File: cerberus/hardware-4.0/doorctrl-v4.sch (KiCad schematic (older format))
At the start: 6 parts, among them CON1 AVR-ISP-6, CON2 AVR-JTAG-10, IC1 ATMEGA324P-A, X1 12 MHz

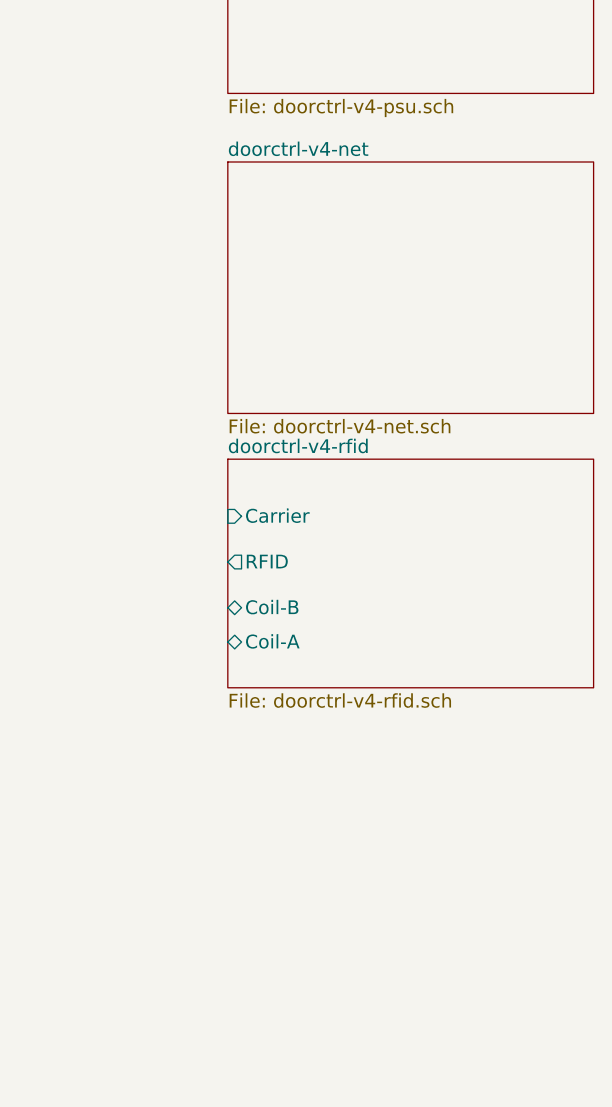
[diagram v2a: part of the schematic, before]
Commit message: Added RS-485 transciever and connectors
git-svn-id: file:///home/ff/projects/osaa/svn@216 a092026d-3e22-4cff-94a7-eaa6fdd35d37
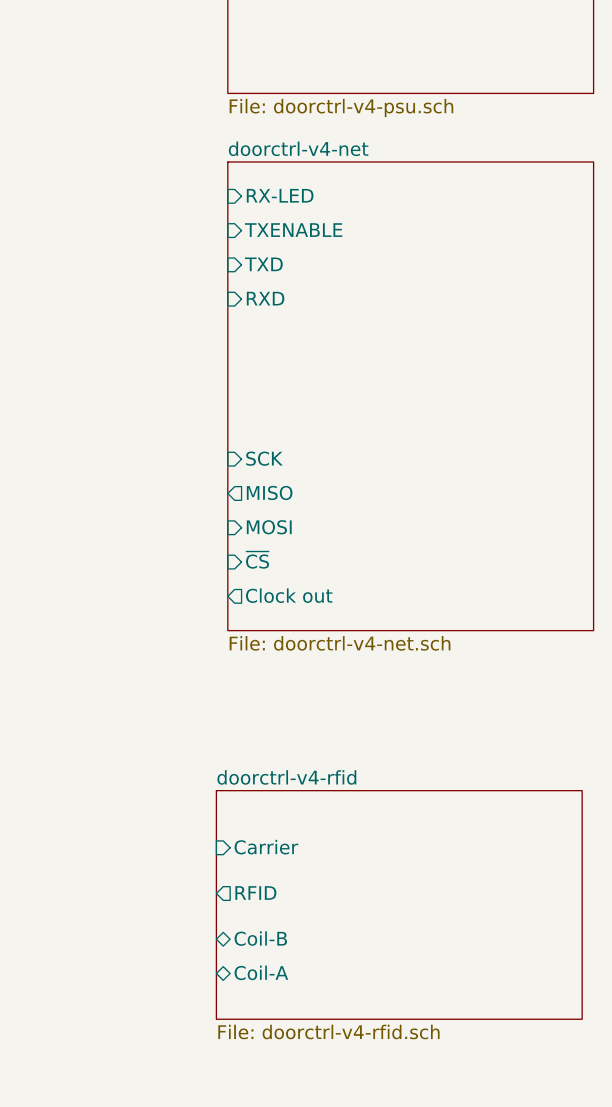
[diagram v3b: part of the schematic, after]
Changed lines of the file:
@@
-EESchema Schematic File Version 2  date 2010-12-15T21:23:41 CET
+EESchema Schematic File Version 2  date 2010-12-16T22:33:40 CET
 LIBS:enc28j60
 LIBS:power
@@
 LIBS:g5sb
 LIBS:pulse-pe-68517-ethernet-trafo
+LIBS:sn65hvd1x
 LIBS:doorctrl-v4-cache
 EELAYER 24  0
@@
 Sheet 1 5
 Title ""
-Date "15 dec 2010"
+Date "16 dec 2010"
 Rev ""
 Comp ""
@@
 $EndSheet
 $Sheet
-S 9300 3400 1600 1000
+S 9250 4850 1600 1000
 U 4CFD3072
 F0 "doorctrl-v4-rfid" 60
 F1 "doorctrl-v4-rfid.sch" 60
-F2 "RFID" O L 9300 3850 60
-F3 "Coil-B" B L 9300 4050 60
-F4 "Coil-A" B L 9300 4200 60
-F5 "Carrier" I L 9300 3650 60
+F2 "RFID" O L 9250 5300 60
+F3 "Coil-B" B L 9250 5500 60
+F4 "Coil-A" B L 9250 5650 60
+F5 "Carrier" I L 9250 5100 60
 $EndSheet
 $Sheet
@@
 $EndSheet
 $Sheet
-S 9300 2100 1600 1100
+S 9300 2100 1600 2050
 U 4CFD2FB8
 F0 "doorctrl-v4-net" 60
 F1 "doorctrl-v4-net.sch" 60
+F2 "RX-LED" I L 9300 2250 60
+F3 "TXENABLE" I L 9300 2400 60
+F4 "TXD" I L 9300 2550 60
+F5 "RXD" I L 9300 2700 60
+F6 "SCK" I L 9300 3400 60
+F7 "MISO" O L 9300 3550 60
+F8 "MOSI" I L 9300 3700 60
+F9 "~CS" I L 9300 3850 60
+F10 "Clock out" O L 9300 4000 60
 $EndSheet
 NoConn ~ 3300 5900
@@
 PB5
 $Comp
-L +3.3V #PWR01
+L +3.3V #PWR4
 U 1 1 4CFAB301
 P 2150 2275
-F 0 "#PWR01" H 2150 2235 30  0001 C CNN
+F 0 "#PWR4" H 2150 2235 30  0001 C CNN
 F 1 "+3.3V" H 2150 2385 30  0000 C CNN
 	1    2150 2275
@@
 $EndComp
 $Comp
-L GND #PWR02
+L GND #PWR3
 U 1 1 4CFAB0A0
 P 1850 2475
-F 0 "#PWR02" H 1850 2475 30  0001 C CNN
+F 0 "#PWR3" H 1850 2475 30  0001 C CNN
 F 1 "GND" H 1850 2405 30  0001 C CNN
 	1    1850 2475
@@
 $EndComp
 $Comp
-L GND #PWR03
+L GND #PWR1
 U 1 1 4CFAB098
 P 1050 2475
-F 0 "#PWR03" H 1050 2475 30  0001 C CNN
+F 0 "#PWR1" H 1050 2475 30  0001 C CNN
 F 1 "GND" H 1050 2405 30  0001 C CNN
 	1    1050 2475
@@
 PC2
 $Comp
-L +3.3V #PWR04
+L +3.3V #PWR7
 U 1 1 4CFA7FD7
 P 3675 5700
-F 0 "#PWR04" H 3675 5660 30  0001 C CNN
+F 0 "#PWR7" H 3675 5660 30  0001 C CNN
 F 1 "+3.3V" H 3675 5810 30  0000 C CNN
 	1    3675 5700
@@
 $EndComp
 $Comp
-L +3.3V #PWR05
+L +3.3V #PWR2
 U 1 1 4CFA5CC7
 P 1800 5600
-F 0 "#PWR05" H 1800 5560 30  0001 C CNN
+F 0 "#PWR2" H 1800 5560 30  0001 C CNN
 F 1 "+3.3V" H 1800 5710 30  0000 C CNN
 	1    1800 5600
@@
 RESET
 $Comp
-L GND #PWR06
+L GND #PWR5
 U 1 1 4CF6BFD7
 P 3050 5075
-F 0 "#PWR06" H 3050 5075 30  0001 C CNN
+F 0 "#PWR5" H 3050 5075 30  0001 C CNN
 F 1 "GND" H 3050 5005 30  0001 C CNN
 	1    3050 5075
@@
 $EndComp
 $Comp
-L +3.3V #PWR07
+L +3.3V #PWR6
 U 1 1 4CF6BFC6
 P 3125 675
-F 0 "#PWR07" H 3125 635 30  0001 C CNN
+F 0 "#PWR6" H 3125 635 30  0001 C CNN
 F 1 "+3.3V" H 3125 785 30  0000 C CNN
 	1    3125 675

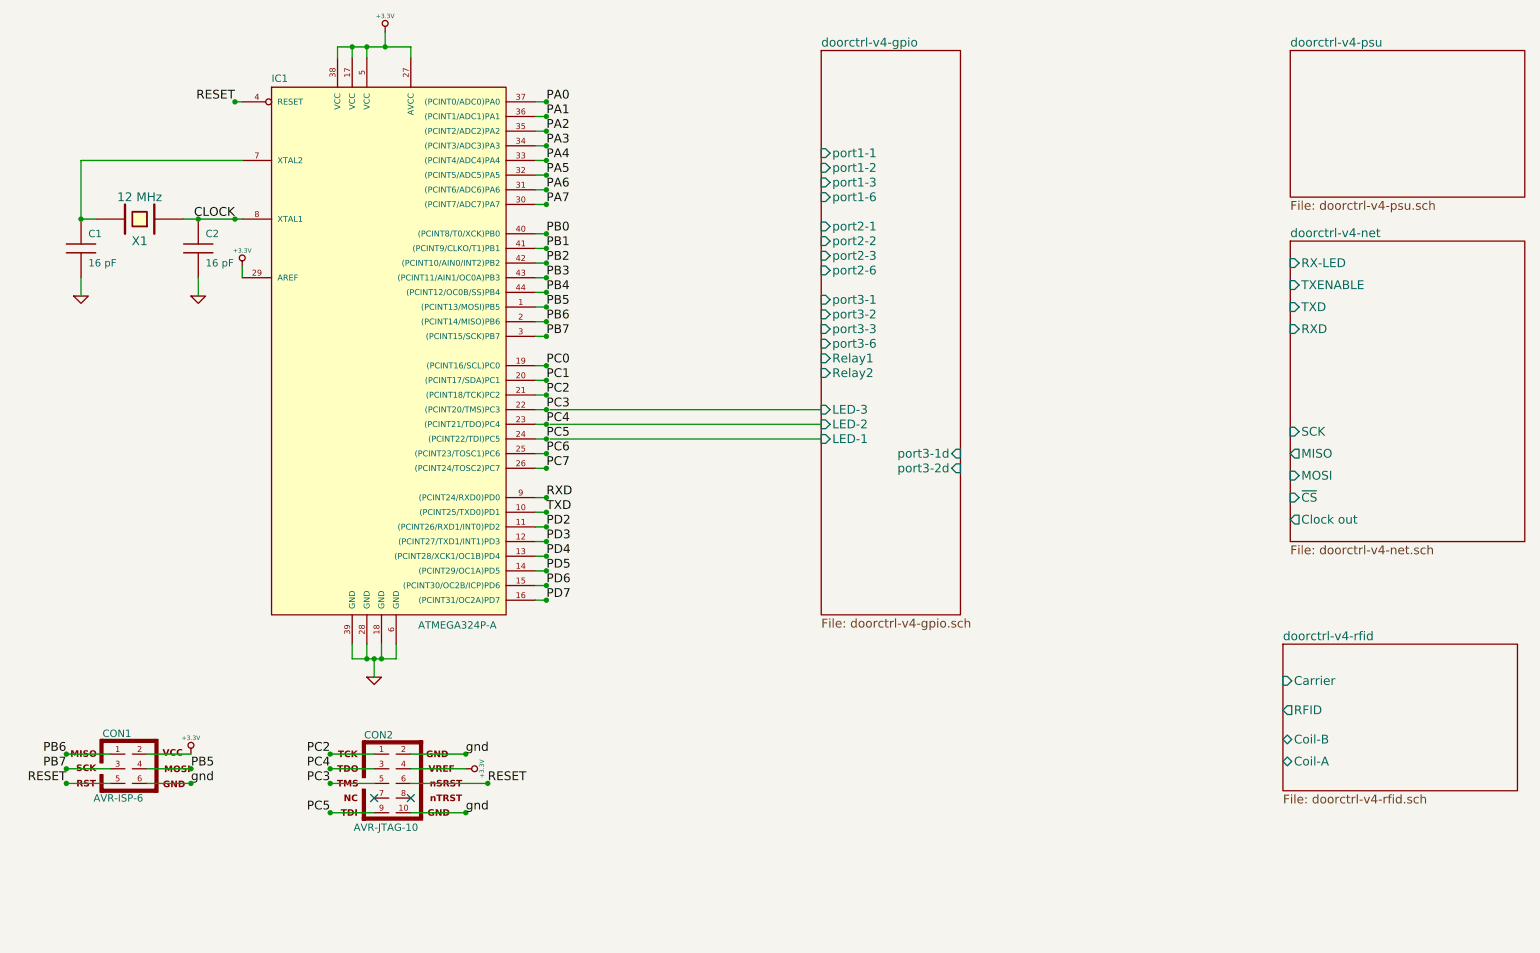
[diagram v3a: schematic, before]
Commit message: Added a 5V regulator for most stuff, except ENC28J60 which lives on its own 3.3v supply
git-svn-id: file:///home/ff/projects/osaa/svn@217 a092026d-3e22-4cff-94a7-eaa6fdd35d37
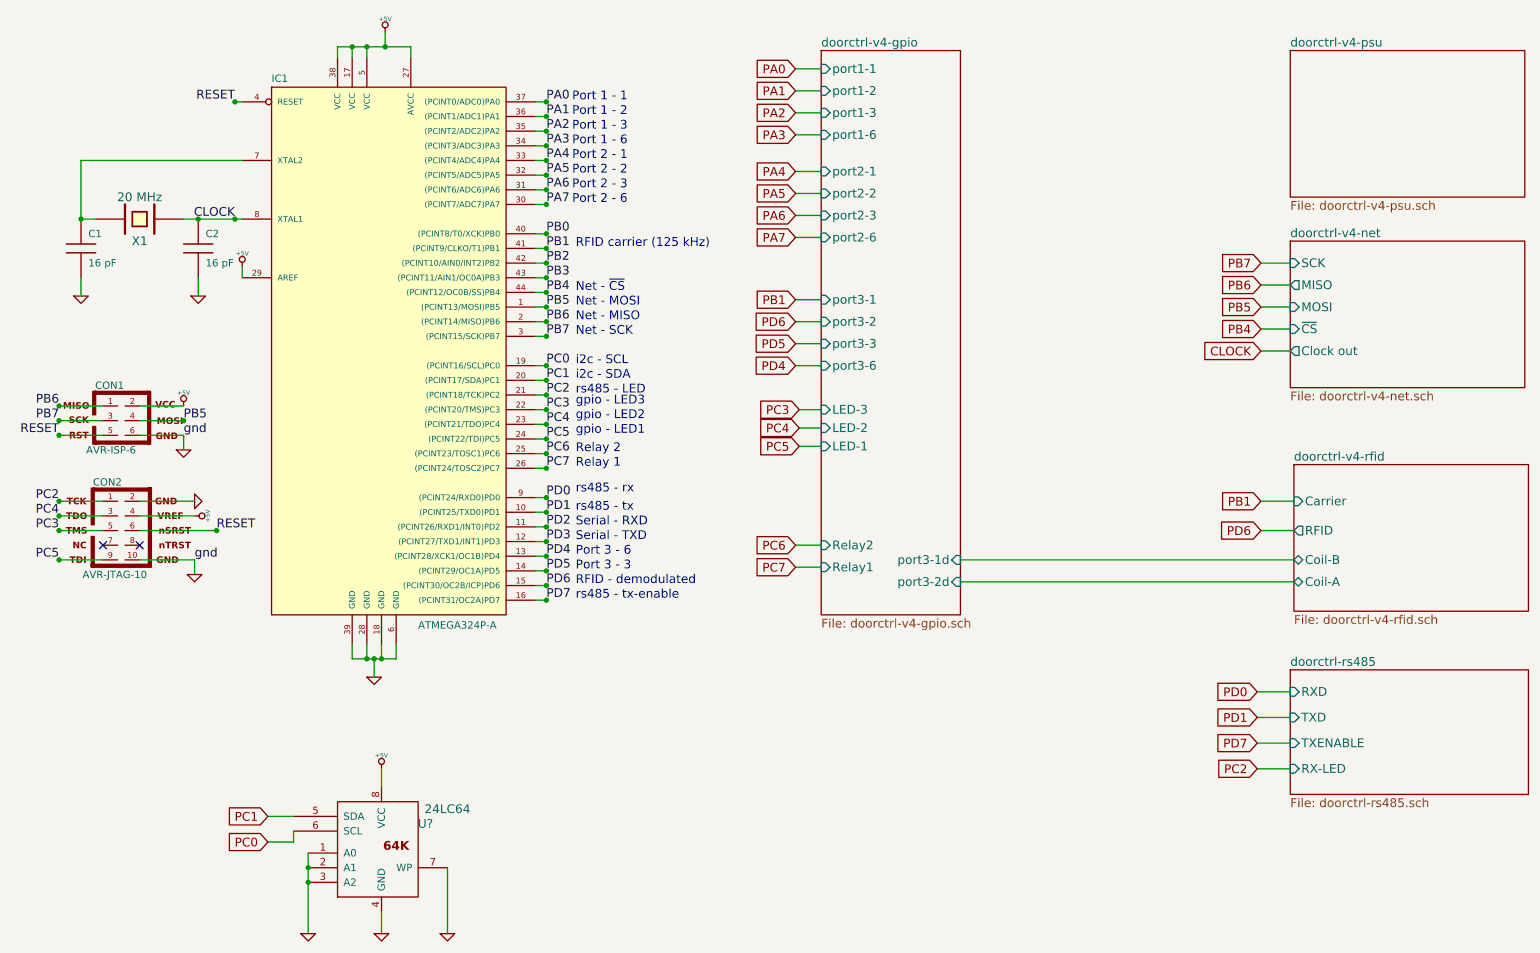
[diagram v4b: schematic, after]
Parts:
- added U?: 24LC64, symbol 24LC64
- X1: value 12 MHz -> 20 MHz
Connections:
- net labels added: +5V, PD0, PD1
- net labels removed: +3.3V, RXD, TXD
- wire segments 69 -> 105
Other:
- note added: "Net - MISO"
- note added: "Net - MOSI"
- note added: "Net - SCK"
- note added: "Net - ~CS"
- note added: "Port 1 - 1"
- note added: "Port 1 - 2"
- note added: "Port 1 - 3"
- note added: "Port 1 - 6"
- note added: "Port 2 - 1"
- note added: "Port 2 - 2"
- note added: "Port 2 - 3"
- note added: "Port 2 - 6"
- note added: "Port 3 - 3"
- note added: "Port 3 - 6"
- note added: "RFID - demodulated"
- note added: "RFID carrier (125 kHz)"
- note added: "Relay 1"
- note added: "Relay 2"
- note added: "Serial - RXD"
- note added: "Serial - TXD"
- note added: "gpio - LED1"
- note added: "gpio - LED2"
- note added: "gpio - LED3"
- note added: "i2c - SCL"
- note added: "i2c - SDA"
- note added: "rs485 - LED"
- note added: "rs485 - rx"
- note added: "rs485 - tx"
- note added: "rs485 - tx-enable"
- moved on the sheet: CON1, CON2

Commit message: Misc labeling
git-svn-id: file:///home/ff/projects/osaa/svn@219 a092026d-3e22-4cff-94a7-eaa6fdd35d37
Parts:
- gave numbers to parts that had none: 1
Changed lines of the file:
@@
-EESchema Schematic File Version 2  date 2010-12-17T21:22:49 CET
+EESchema Schematic File Version 2  date 2010-12-17T21:31:15 CET
 LIBS:enc28j60
 LIBS:power
@@
 PB7
 $Comp
-L +5V #PWR?
+L +5V #PWR8
 U 1 1 4D0BBC2E
 P 2150 2275
-F 0 "#PWR?" H 2150 2365 20  0001 C CNN
+F 0 "#PWR8" H 2150 2365 20  0001 C CNN
 F 1 "+5V" H 2150 2365 30  0000 C CNN
 	1    2150 2275
@@
 PC1
 $Comp
-L +5V #PWR?
+L +5V #PWR11
 U 1 1 4D0BB852
 P 3100 5700
-F 0 "#PWR?" H 3100 5790 20  0001 C CNN
+F 0 "#PWR11" H 3100 5790 20  0001 C CNN
 F 1 "+5V" H 3100 5790 30  0000 C CNN
 	1    3100 5700
@@
 $EndComp
 $Comp
-L GND #PWR?
+L GND #PWR9
 U 1 1 4D0BB830
 P 2600 6825
-F 0 "#PWR?" H 2600 6825 30  0001 C CNN
+F 0 "#PWR9" H 2600 6825 30  0001 C CNN
 F 1 "GND" H 2600 6755 30  0001 C CNN
 	1    2600 6825
@@
 $EndComp
 $Comp
-L GND #PWR?
+L GND #PWR12
 U 1 1 4D0BB82C
 P 3100 6825
-F 0 "#PWR?" H 3100 6825 30  0001 C CNN
+F 0 "#PWR12" H 3100 6825 30  0001 C CNN
 F 1 "GND" H 3100 6755 30  0001 C CNN
 	1    3100 6825
@@
 $EndComp
 $Comp
-L GND #PWR?
+L GND #PWR14
 U 1 1 4D0BB822
 P 3550 6825
-F 0 "#PWR?" H 3550 6825 30  0001 C CNN
+F 0 "#PWR14" H 3550 6825 30  0001 C CNN
 F 1 "GND" H 3550 6755 30  0001 C CNN
 	1    3550 6825
@@
 $EndComp
 $Comp
-L 24LC64 U?
+L 24LC64 U8
 U 1 1 4D0BB80A
 P 3100 6275
-F 0 "U?" H 3400 6475 60  0000 C CNN
+F 0 "U8" H 3400 6475 60  0000 C CNN
 F 1 "24LC64" H 3550 6575 60  0000 C CNN
 	1    3100 6275
@@
 $EndSheet
 $Comp
-L GND #PWR8
+L GND #PWR4
 U 1 1 4D0BAF81
 P 1825 3875
-F 0 "#PWR8" H 1825 3875 30  0001 C CNN
+F 0 "#PWR4" H 1825 3875 30  0001 C CNN
 F 1 "GND" H 1825 3805 30  0001 C CNN
 	1    1825 3875
@@
 $EndComp
 $Comp
-L +5V #PWR9
+L +5V #PWR5
 U 1 1 4D0BAF77
 P 1825 3975
-F 0 "#PWR9" H 1825 4065 20  0001 C CNN
+F 0 "#PWR5" H 1825 4065 20  0001 C CNN
 F 1 "+5V" H 1825 4065 30  0000 C CNN
 	1    1825 3975
@@
 $EndComp
 $Comp
-L GND #PWR10
+L GND #PWR6
 U 1 1 4D0BAF62
 P 1825 4375
-F 0 "#PWR10" H 1825 4375 30  0001 C CNN
+F 0 "#PWR6" H 1825 4375 30  0001 C CNN
 F 1 "GND" H 1825 4305 30  0001 C CNN
 	1    1825 4375
@@
 $EndComp
 $Comp
-L +5V #PWR7
+L +5V #PWR13
 U 1 1 4D0BAF41
 P 3125 675
-F 0 "#PWR7" H 3125 765 20  0001 C CNN
+F 0 "#PWR13" H 3125 765 20  0001 C CNN
 F 1 "+5V" H 3125 765 30  0000 C CNN
 	1    3125 675
@@
 PB5
 $Comp
-L GND #PWR4
+L GND #PWR7
 U 1 1 4CFAB0A0
 P 1850 2475
-F 0 "#PWR4" H 1850 2475 30  0001 C CNN
+F 0 "#PWR7" H 1850 2475 30  0001 C CNN
 F 1 "GND" H 1850 2405 30  0001 C CNN
 	1    1850 2475
@@
 RESET
 $Comp
-L GND #PWR6
+L GND #PWR10
 U 1 1 4CF6BFD7
 P 3050 5075
-F 0 "#PWR6" H 3050 5075 30  0001 C CNN
+F 0 "#PWR10" H 3050 5075 30  0001 C CNN
 F 1 "GND" H 3050 5005 30  0001 C CNN
 	1    3050 5075
